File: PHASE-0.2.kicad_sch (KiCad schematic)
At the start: 0 parts

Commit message: Schematic Design
I²C and I²S connection haven't been implemented on the schematic, will add them after pin configuration was done.
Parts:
- added C1, C13, C15, C3, C8: 10u, Capacitor_SMD:C_0603_1608Metric, symbol Device:C
- added C10, C17: 22u, Capacitor_SMD:C_0603_1608Metric, symbol Device:C
- added C11, C12, C14, C16, C18, C19, C2, C4, C5, C6, C7, C9: 100n, Capacitor_SMD:C_0402_1005Metric, symbol Device:C
- added C20: 47p, Capacitor_SMD:C_0402_1005Metric, symbol Device:C
- added C21, C22: 1u, Capacitor_SMD:C_0402_1005Metric, symbol Device:C
- added H1, H2, H3, H4: MountingHole, MountingHole:MountingHole_3.2mm_M3, symbol Mechanical:MountingHole
- added J1: Conn_02x10_Top_Bottom, Connector_PinHeader_2.54mm:PinHeader_2x10_P2.54mm_Vertical, symbol Connector_Generic:Conn_02x10_Top_Bottom
- added J2: USB_B, Connector_USB:USB_B_Lumberg_2411_02_Horizontal, symbol Connector:USB_B
- added L1: 4.7u, Inductor_SMD:L_Murata_DFE201610P, symbol Device:L
- added U1: LPC5528JBD64, utils:TQFP-64-1EP_10x10mm_P0.5mm_EP3.6x3.6mm, symbol utils:LPC5528JBD64
- added U2: XC6206PxxxMR, Package_TO_SOT_SMD:SOT-23-3, symbol Regulator_Linear:XC6206PxxxMR
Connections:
- new net: L1.1, U1.31 (LX)
- new net CLK: J1.4 (Pin_4)
- new net DATA: J1.3 (Pin_3)
- new net DSD: J1.16 (Pin_16)
- new net DSDON: J1.7 (Pin_7)
- new net F0: J1.17 (Pin_17)
- new net F1: J1.18 (Pin_18)
- new net F2: J1.19 (Pin_19)
- new net F3: J1.20 (Pin_20)
- new net FSCLK: J1.5 (Pin_5)
- new net GND: J1.8 (Pin_8)
- new net GNDD: C1.2, C10.2, C11.2, C12.2, C13.2, C14.2, C15.2, C16.2, C17.2, C18.2, C19.2, C2.2, C20.2, C21.2, C22.2, C3.2, C4.2, C5.2, C6.2, C7.2, C8.2, C9.2, J1.13 (Pin_13), J1.14 (Pin_14), J1.15 (Pin_15), J2.4 (GND), J2.SH (Shield), U1.11 (VSSA), U1.22 (USB1_VSS), U1.26 (USB1_VSS), U1.27 (USB1_3V3), U1.30 (VSS_DCDC), U1.64 (USB0_VSS), U1.65 (VSS), U2.1 (GND)
- new net MCLK: J1.6 (Pin_6)
- new net MUTE: J1.11 (Pin_11)
- new net PLUG: J1.1 (Pin_1)
- new net RESETN: U1.21 (RESETN)
- new net SCL: J1.2 (Pin_2)
- new net SDA: J1.12 (Pin_12)
- new net USB0_DM: U1.63 (USB0_DM)
- new net USB0_DP: U1.62 (USB0_DP)
- new net USB1_DM: J2.2 (D-), U1.24 (USB1_DM)
- new net USB1_DP: J2.3 (D+), U1.23 (USB1_DP)
- new net VBUS: C21.1, J2.1 (VBUS), U1.25 (USB1_VBUS), U2.3 (VI)
- new net VCC: C1.1, C10.1, C11.1, C12.1, C13.1, C14.1, C15.1, C16.1, C17.1, C18.1, C19.1, C2.1, C20.1, C22.1, C3.1, C4.1, C5.1, C6.1, C7.1, C8.1, C9.1, J1.10 (Pin_10), J1.9 (Pin_9), L1.2, U1.10 (VREFP), U1.16 (VDD), U1.28 (VDD_PMU), U1.29 (FB), U1.32 (VBAT_DCDC), U1.33 (VBAT_PMU), U1.43 (VDD), U1.54 (VDD), U1.61 (USB0_3V3), U1.8 (VDD), U1.9 (VDDA), U2.2 (VO)
- new net XI: U1.20 (XTAL32M_P)
- new net XO: U1.19 (XTAL32M_N)
- no-connect marks 0 -> 2

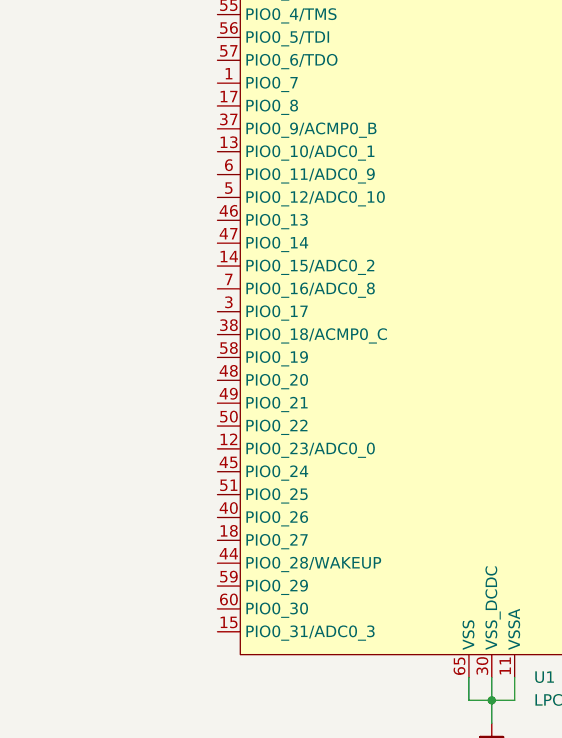
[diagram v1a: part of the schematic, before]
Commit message: Update PHASE-0.2.kicad_sch
Arranged pinout for I2S and I2C,etc.
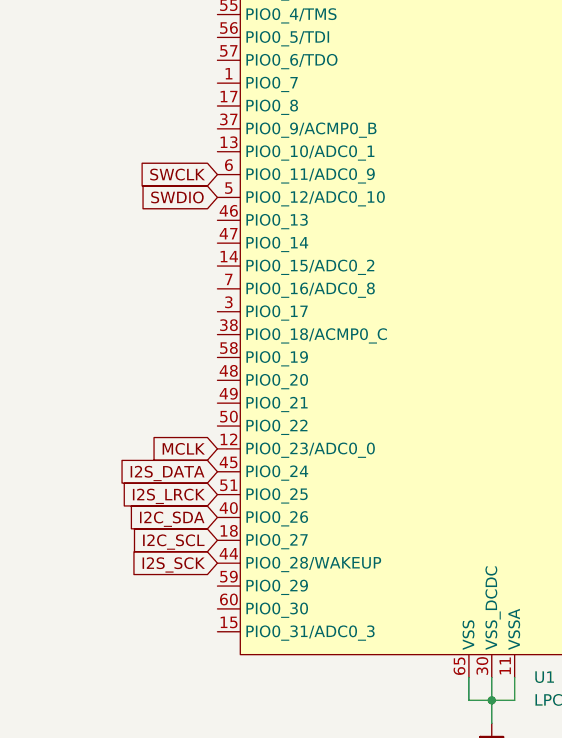
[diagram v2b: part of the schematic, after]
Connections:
- net MCLK: now also U1.12 (PIO0_23/ADC0_0)
- net I2C_SCL: now reaches U1.18 (PIO0_27)
- net I2C_SDA: now reaches U1.40 (PIO0_26)
- net I2S_SCK: now reaches U1.44 (PIO0_28/WAKEUP)
- net I2S_DATA: now reaches U1.45 (PIO0_24)
- net SWDIO: now reaches U1.5 (PIO0_12/ADC0_10)
- net I2S_LRCK: now reaches U1.51 (PIO0_25)
- net SWCLK: now reaches U1.6 (PIO0_11/ADC0_9)
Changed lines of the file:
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@@
+		)
+	)
+	(global_label "I2S_LRCK"
+		(shape input)
+		(at 144.78 130.81 180)
+		(fields_autoplaced yes)
+		(effects
+			(font
+				(size 1.27 1.27)
+			)
+			(justify right)
+		)
+		(property "Intersheetrefs" "${INTERSHEET_REFS}"
+			(at 132.9653 130.81 0)
+			(hide yes)
+			(show_name no)
+			(do_not_autoplace no)
+			(effects
+				(font
+					(size 1.27 1.27)
+				)
+				(justify right)
+			)
+		)
+	)
+	(global_label "I2C_SDA"
+		(shape input)
+		(at 144.78 133.35 180)
+		(fields_autoplaced yes)
+		(effects
+			(font
+				(size 1.27 1.27)
+			)
+			(justify right)
+		)
+		(property "Intersheetrefs" "${INTERSHEET_REFS}"
+			(at 134.1748 133.35 0)
+			(hide yes)
+			(show_name no)
+			(do_not_autoplace no)
+			(effects
+				(font
+					(size 1.27 1.27)
+				)
+				(justify right)
+			)
 		)
 	)
@@
 		)
 	)
+	(global_label "MCLK"
+		(shape input)
+		(at 144.78 125.73 180)
+		(fields_autoplaced yes)
+		(effects
+			(font
+				(size 1.27 1.27)
+			)
+			(justify right)
+		)
+		(property "Intersheetrefs" "${INTERSHEET_REFS}"
+			(at 136.7753 125.73 0)
+			(hide yes)
+			(show_name no)
+			(do_not_autoplace no)
+			(effects
+				(font
+					(size 1.27 1.27)
+				)
+				(justify right)
+			)
+		)
+	)
 	(global_label "MUTE"
 		(shape input)
@@
 		)
 	)
+	(global_label "SWCLK"
+		(shape input)
+		(at 144.78 95.25 180)
+		(fields_autoplaced yes)
+		(effects
+			(font
+				(size 1.27 1.27)
+			)
+			(justify right)
+		)
+		(property "Intersheetrefs" "${INTERSHEET_REFS}"
+			(at 135.5658 95.25 0)
+			(hide yes)
+			(show_name no)
+			(do_not_autoplace no)
+			(effects
+				(font
+					(size 1.27 1.27)
+				)
+				(justify right)
+			)
+		)
+	)
 	(global_label "CLK"
 		(shape input)
@@
 		)
 	)
+	(global_label "SWDIO"
+		(shape input)
+		(at 144.78 97.79 180)
+		(fields_autoplaced yes)
+		(effects
+			(font
+				(size 1.27 1.27)
+			)
+			(justify right)
+		)
+		(property "Intersheetrefs" "${INTERSHEET_REFS}"
+			(at 135.9286 97.79 0)
+			(hide yes)
+			(show_name no)
+			(do_not_autoplace no)
+			(effects
+				(font
+					(size 1.27 1.27)
+				)
+				(justify right)
+			)
+		)
+	)
 	(global_label "USB0_DM"
 		(shape input)
@@
 		)
 	)
+	(global_label "I2S_SCK"
+		(shape input)
+		(at 144.78 138.43 180)
+		(fields_autoplaced yes)
+		(effects
+			(font
+				(size 1.27 1.27)
+			)
+			(justify right)
+		)
+		(property "Intersheetrefs" "${INTERSHEET_REFS}"
+			(at 134.0539 138.43 0)
+			(hide yes)
+			(show_name no)
+			(do_not_autoplace no)
+			(effects
+				(font
+					(size 1.27 1.27)
+				)
+				(justify right)
+			)
+		)
+	)
 	(global_label "USB1_DP"
 		(shape input)
@@
 		)
 	)
+	(global_label "I2S_DATA"
+		(shape input)
+		(at 144.78 128.27 180)
+		(fields_autoplaced yes)
+		(effects
+			(font
+				(size 1.27 1.27)
+			)
+			(justify right)
+		)
+		(property "Intersheetrefs" "${INTERSHEET_REFS}"
+			(at 133.3886 128.27 0)
+			(hide yes)
+			(show_name no)
+			(do_not_autoplace no)
+			(effects
+				(font
+					(size 1.27 1.27)
+				)
+				(justify right)
+			)
+		)
+	)
 	(global_label "DSDON"
 		(shape input)
@@
 			)
 		)
+	)
+	(global_label "I2C_SCL"
+		(shape input)
+		(at 144.78 135.89 180)
+		(fields_autoplaced yes)
+		(effects
+			(font
+				(size 1.27 1.27)
+			)
+			(justify right)
+		)
+		(property "Intersheetrefs" "${INTERSHEET_REFS}"
+			(at 134.2353 135.89 0)
+			(hide yes)
+			(show_name no)
+			(do_not_autoplace no)
+			(effects
+				(font
+					(size 1.27 1.27)
+				)
+				(justify right)
+			)
+		)

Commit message: Schematic and PCB Design
-Changed mounting hole size from M3 to M2
-Initial PCB Layout
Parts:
- H1, H2, H3, H4: footprint MountingHole:MountingHole_3.2mm_M3 -> MountingHole:MountingHole_2.2mm_M2
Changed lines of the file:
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@@
 			)
 		)
-		(property "Footprint" "MountingHole:MountingHole_3.2mm_M3"
+		(property "Footprint" "MountingHole:MountingHole_2.2mm_M2"
 			(at 132.08 27.94 0)
 			(hide yes)
@@
 			)
 		)
-		(property "Footprint" "MountingHole:MountingHole_3.2mm_M3"
+		(property "Footprint" "MountingHole:MountingHole_2.2mm_M2"
 			(at 132.08 22.86 0)
 			(hide yes)
@@
 			)
 		)
-		(property "Footprint" "MountingHole:MountingHole_3.2mm_M3"
+		(property "Footprint" "MountingHole:MountingHole_2.2mm_M2"
 			(at 132.08 33.02 0)
 			(hide yes)
@@
 			)
 		)
-		(property "Footprint" "MountingHole:MountingHole_3.2mm_M3"
+		(property "Footprint" "MountingHole:MountingHole_2.2mm_M2"
 			(at 132.08 17.78 0)
 			(hide yes)
